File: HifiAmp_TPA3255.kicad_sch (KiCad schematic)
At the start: 123 parts, among them J1 PVDD 48V IN — NEEDS_DATA, J2 RCA L SE, J3 RCA R SE, J301 SPK_L, J302 SPK_R, J4 VOLUME_REMOTE, Q301 IPP330P10NM, Q302 IXTK200N10L2, U1 LM5010ASD, U2 LM2940IMP-12/NOPB, U3 TLV1117-33IDCY, U4 OPA1612AIDR, U5 OPA1612AIDR, U6 TPA3255B, U7 TPS3802K33DCKR, U8 LM5069-2

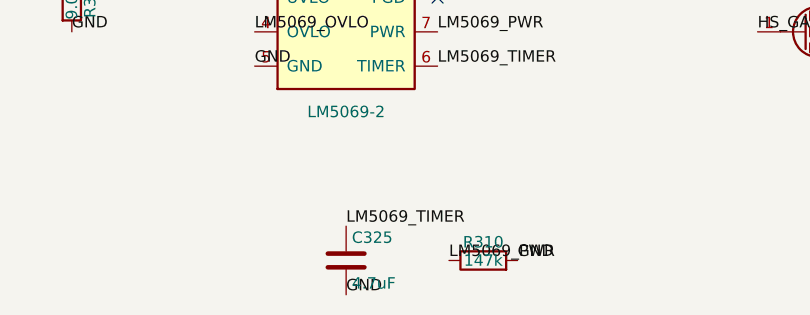
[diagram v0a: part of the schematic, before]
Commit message: fix(schematic): restore the real WIMA part for C325 and widen its footprint (D1.7)
D1.5 had rejected MKS2C044701O00KSSD as an invented part, reading the "O"
as a tolerance code. It is not one. A WIMA part number puts the box and
pitch in fields 11-12 and the tolerance in field 15 alone, so the "O" is
the second character of box code 1O and the tolerance is the "K" in KSSD.

The rejected part is the real one, and its replacement is the invented
one: B0 is not a WIMA voltage code (MKS2 spans 63 to 630 VDC with no 50 V
rating) and box 1K, 7.2 x 13 mm, only holds 2.2 uF.

Reading the catalogue also breaks the dimension assumption. At 5 mm pitch
the constant of the MKS2 series is the LENGTH, 7.2 mm, never the
thickness. The 4.7 uF box is 11 x 18 x 7.2 mm, so the W7.2mm footprint
was 3.8 mm too narrow and the part would not have fitted.

C325 now carries MKS2C044701O00KSSD, value 4.7uF/63V, and the stock
footprint C_Rect_L7.2mm_W11.0mm_P5.00mm_FKS2_FKP2_MKS2_MKP2. The x1.41
startup margin holds: +/-10 % is catalogued, only the voltage rating
moves from 50 to 63 V. Written through the MCP, re-read from the file,
position untouched, ERC still 15 warnings and 0 errors.

Two consequences recorded. D1.9 opens: C321-C324 carry the same class of
defect, a 3.5 mm box that cannot hold 680 nF at the 100 V TI requires.
D1.8 loses its blocker, since the local film footprint was redundant with
a stock one all along and only has to be dropped, never repaired.

Co-Authored-By: Claude Opus 5 <noreply@anthropic.com>
Claude-Session: https://claude.ai/code/session_019Lx21MypvErSrEbffS7PFZ
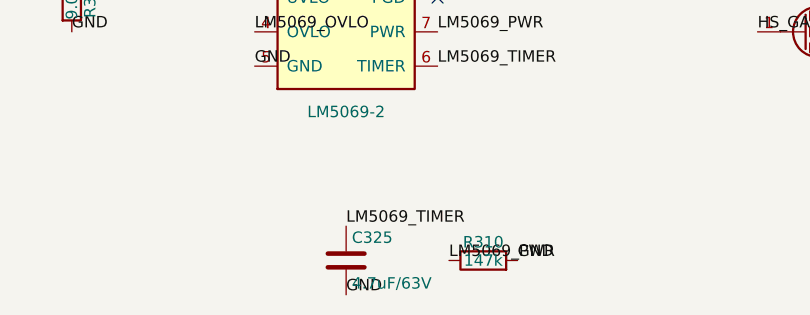
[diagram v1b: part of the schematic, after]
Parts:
- C325: value 4.7uF -> 4.7uF/63V; footprint Capacitor_THT:C_Rect_L7.2mm_W7.2mm_P5.00mm_FKS2_FKP2_MKS2_MKP2 -> Capacitor_THT:C_Rect_L7.2mm_W11.0mm_P5.00mm_FKS2_FKP2_MKS2_MKP2; MPN MKS2B044701K00KSSD -> MKS2C044701O00KSSD
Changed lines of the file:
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@@
 			)
 		)
-		(property "Value" "4.7uF"
+		(property "Value" "4.7uF/63V"
 			(at 330.835 452.12 0)
 			(effects
@@
 			)
 		)
-		(property "Footprint" "Capacitor_THT:C_Rect_L7.2mm_W7.2mm_P5.00mm_FKS2_FKP2_MKS2_MKP2"
+		(property "Footprint" "Capacitor_THT:C_Rect_L7.2mm_W11.0mm_P5.00mm_FKS2_FKP2_MKS2_MKP2"
 			(at 331.1652 453.39 0)
 			(hide yes)
@@
 			)
 		)
-				(property "MPN" "MKS2B044701K00KSSD"
+				(property "MPN" "MKS2C044701O00KSSD"
 			(at 330.2 449.58 0)
 			(effects (font (size 1.27 1.27)) (hide yes))

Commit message: fix(schematic): give the four 1500 uF bulks the diameter the EVM actually uses (D1.11)
C312 to C315 carried CP_Radial_D16.0mm_P7.50mm. The TPA3255EVM bill of
materials, which docs/architecture.md names as the anchor for this bulk,
lists EEU-FC1J152 in an 18 mm diameter can. The footprint was 2 mm too
narrow -- the fourth footprint in this project resting on a dimension that
was assumed rather than read.

C316 and C317 came out clean: the EVM lists SLPX472M080H3P3, "D35 mm x
L30", the CDE type SLP part-number key resolves H3 to 35 x 30 mm, and the
CDE mounting-hole drawing prescribes a 10.0 mm pitch with two 2.0 mm
holes -- so the KiCad 2.0 mm drill is the prescribed hole, not a zero
clearance on a 2.0 mm pin.

Footprint write read back from the file, positions untouched, ERC still at
15 violations and 0 errors.

Co-Authored-By: Claude Opus 5 <noreply@anthropic.com>
Claude-Session: https://claude.ai/code/session_01SP8MCxRp77nUWzHqJxRtmC
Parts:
- C312, C313, C314, C315: footprint Capacitor_THT:CP_Radial_D16.0mm_P7.50mm -> Capacitor_THT:CP_Radial_D18.0mm_P7.50mm
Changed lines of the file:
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@@
 			)
 		)
-		(property "Footprint" "Capacitor_THT:CP_Radial_D16.0mm_P7.50mm"
+		(property "Footprint" "Capacitor_THT:CP_Radial_D18.0mm_P7.50mm"
 			(at 394.6652 303.53 0)
 			(hide yes)
@@
 			)
 		)
-		(property "Footprint" "Capacitor_THT:CP_Radial_D16.0mm_P7.50mm"
+		(property "Footprint" "Capacitor_THT:CP_Radial_D18.0mm_P7.50mm"
 			(at 407.3652 303.53 0)
 			(hide yes)
@@
 			)
 		)
-		(property "Footprint" "Capacitor_THT:CP_Radial_D16.0mm_P7.50mm"
+		(property "Footprint" "Capacitor_THT:CP_Radial_D18.0mm_P7.50mm"
 			(at 420.0652 303.53 0)
 			(hide yes)
@@
 			)
 		)
-		(property "Footprint" "Capacitor_THT:CP_Radial_D16.0mm_P7.50mm"
+		(property "Footprint" "Capacitor_THT:CP_Radial_D18.0mm_P7.50mm"
 			(at 432.7652 303.53 0)
 			(hide yes)

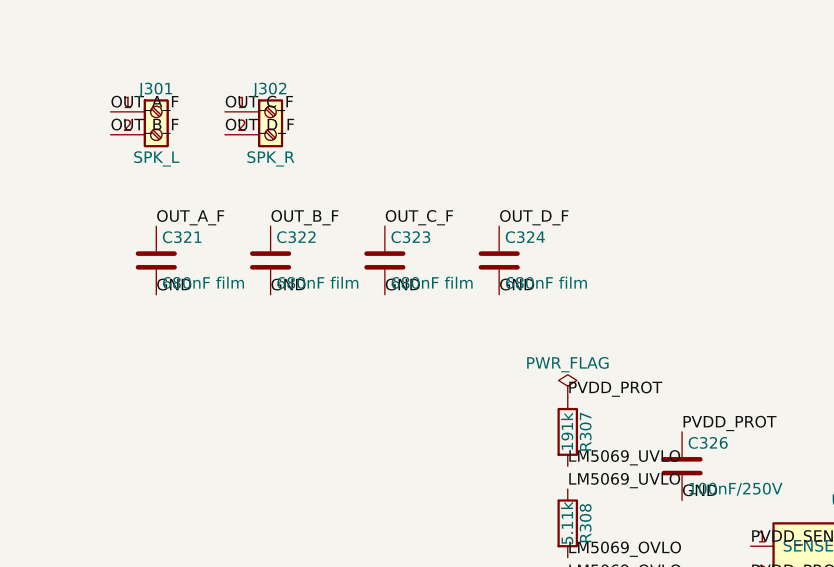
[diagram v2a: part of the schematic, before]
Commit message: fix(schematic): put the output-filter films on the box WIMA actually sells (D1.9)
C321 to C324 carried a 5 mm pitch footprint for a 7.2 x 3.5 mm body. Both
figures were wrong. The TPA3255EVM bill of materials settles the dielectric
first: the EVM uses a KEMET PHE426HB7100JR06, metallized polypropylene,
1 uF/250 V on a 17.5 mm pitch. The WIMA MKP4 catalogue then contradicts the
assumption that no MKP exists below 250 V -- the series starts at 100 VDC --
and lists 0.68 uF in an 8 x 15 x 18 mm box on a 15 mm pitch, the same box at
100 and at 250 VDC. 250 V costs nothing mechanically, so it is what we take.

The four caps move to Capacitor_THT:C_Rect_L18.0mm_W8.0mm_P15.00mm_FKS3_FKP3,
a standard-library footprint whose own description points back at the WIMA
catalogue, and their Value now carries the rating.

This leaves CF_Film_Box_P5.00mm_7.2x3.5mm with no users, so it goes. The
local library keeps only the fuse, and its fp-lib-table entry stays earned.

Writes read back from the file, positions untouched, ERC still at 15
violations and 0 errors with the same message set.

Co-Authored-By: Claude Opus 5 <noreply@anthropic.com>
Claude-Session: https://claude.ai/code/session_01SP8MCxRp77nUWzHqJxRtmC
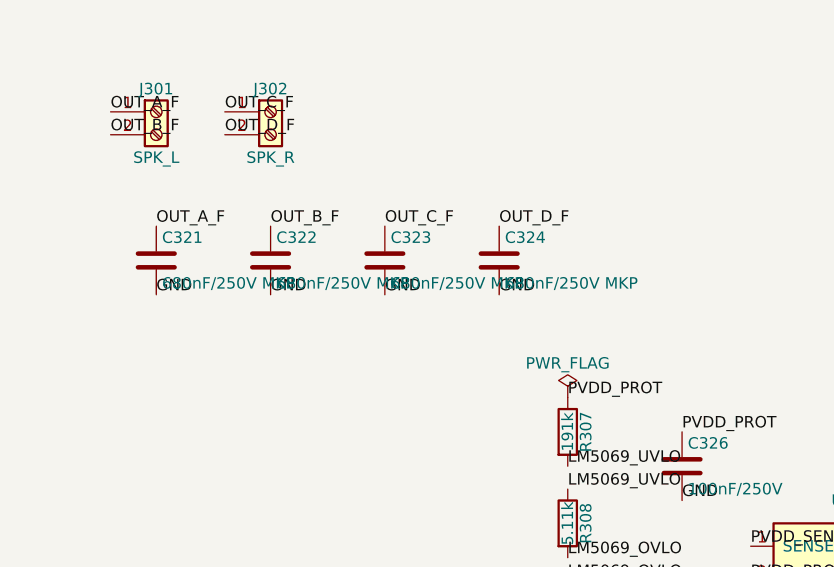
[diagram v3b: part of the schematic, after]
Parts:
- C321, C322, C323, C324: value 680nF film -> 680nF/250V MKP; footprint HifiAmp_TPA3255_Local:CF_Film_Box_P5.00mm_7.2x3.5mm -> Capacitor_THT:C_Rect_L18.0mm_W8.0mm_P15.00mm_FKS3_FKP3
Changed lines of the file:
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@@
 			)
 		)
-		(property "Value" "680nF film"
+		(property "Value" "680nF/250V MKP"
 			(at 254.635 383.54 0)
 			(effects
@@
 			)
 		)
-		(property "Footprint" "HifiAmp_TPA3255_Local:CF_Film_Box_P5.00mm_7.2x3.5mm"
+		(property "Footprint" "Capacitor_THT:C_Rect_L18.0mm_W8.0mm_P15.00mm_FKS3_FKP3"
 			(at 254.9652 384.81 0)
 			(hide yes)
@@
 			)
 		)
-		(property "Value" "680nF film"
+		(property "Value" "680nF/250V MKP"
 			(at 267.335 383.54 0)
 			(effects
@@
 			)
 		)
-		(property "Footprint" "HifiAmp_TPA3255_Local:CF_Film_Box_P5.00mm_7.2x3.5mm"
+		(property "Footprint" "Capacitor_THT:C_Rect_L18.0mm_W8.0mm_P15.00mm_FKS3_FKP3"
 			(at 267.6652 384.81 0)
 			(hide yes)
@@
 			)
 		)
-		(property "Value" "680nF film"
+		(property "Value" "680nF/250V MKP"
 			(at 280.035 383.54 0)
 			(effects
@@
 			)
 		)
-		(property "Footprint" "HifiAmp_TPA3255_Local:CF_Film_Box_P5.00mm_7.2x3.5mm"
+		(property "Footprint" "Capacitor_THT:C_Rect_L18.0mm_W8.0mm_P15.00mm_FKS3_FKP3"
 			(at 280.3652 384.81 0)
 			(hide yes)
@@
 			)
 		)
-		(property "Value" "680nF film"
+		(property "Value" "680nF/250V MKP"
 			(at 292.735 383.54 0)
 			(effects
@@
 			)
 		)
-		(property "Footprint" "HifiAmp_TPA3255_Local:CF_Film_Box_P5.00mm_7.2x3.5mm"
+		(property "Footprint" "Capacitor_THT:C_Rect_L18.0mm_W8.0mm_P15.00mm_FKS3_FKP3"
 			(at 293.0652 384.81 0)
 			(hide yes)

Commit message: feat(schematic): settle the output inductors on a real part (D1.10, D1.12)
L301 to L304 carried Inductor_SMD:L_Wuerth_HCI-1350 with no MPN behind it,
and the stored-energy argument said that can was about half the size the
job needs. The TPA3255EVM bill of materials points at Coilcraft's MA5172-AE,
and that datasheet (document 943) lists PA6331-AE in the same family:
15 uH, 31 mOhm DCR, 20 A Isat, 9.8 A Irms at a 20 C rise. That is our spec
sheet, on a part built for TI Class-D stages. Taken on the user's call.

The real part is a 28.6 x 12.3 mm through-hole toroid standing upright, not
a 12.8 mm SMD can. The datasheet drawing is not to scale -- 2.836 pt/mm in
the front view against 2.463 in profile -- so the labels rule, as with
Schurter: 10.0 +/- 0.5 mm pin spacing, 0.96 to 1.07 mm pins.

No standard footprint fits. Bourns_5700 has the length but an 11.43 mm
spacing, past tolerance; Pulse_D has the spacing but a courtyard 1.9 mm too
short. So the project earns a second local footprint. This time
create_footprint's own graphics came out right -- 0.25 mm around the
outermost feature, silkscreen 0.15 mm clear of the body. CF_Film_Box failed
because of the dimensions it was handed, not because of the generator.

D1.12: fp-lib-table named the local library by an absolute Windows path, so
a clone of this repo anywhere else would have lost both local footprints
without a word. It now uses ${KIPRJMOD}, which sym-lib-table already did.

Footprint and writes read back from the files, ERC still at 15 violations
and 0 errors.

Co-Authored-By: Claude Opus 5 <noreply@anthropic.com>
Claude-Session: https://claude.ai/code/session_01SP8MCxRp77nUWzHqJxRtmC
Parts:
- L301, L302, L303, L304: value 15uH -> 15uH/20A; footprint Inductor_SMD:L_Wuerth_HCI-1350 -> HifiAmp_TPA3255_Local:L_Toroid_Vertical_L28.6mm_W12.3mm_P10.00mm_Coilcraft_PA6331
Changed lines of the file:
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@@
 			)
 		)
-		(property "Value" "15uH"
+		(property "Value" "15uH/20A"
 			(at 255.905 345.44 90)
 			(effects
@@
 			)
 		)
-		(property "Footprint" "Inductor_SMD:L_Wuerth_HCI-1350"
+		(property "Footprint" "HifiAmp_TPA3255_Local:L_Toroid_Vertical_L28.6mm_W12.3mm_P10.00mm_Coilcraft_PA6331"
 			(at 254 345.44 0)
 			(hide yes)
@@
 			)
 		)
-		(property "Value" "15uH"
+		(property "Value" "15uH/20A"
 			(at 268.605 345.44 90)
 			(effects
@@
 			)
 		)
-		(property "Footprint" "Inductor_SMD:L_Wuerth_HCI-1350"
+		(property "Footprint" "HifiAmp_TPA3255_Local:L_Toroid_Vertical_L28.6mm_W12.3mm_P10.00mm_Coilcraft_PA6331"
 			(at 266.7 345.44 0)
 			(hide yes)
@@
 			)
 		)
-		(property "Value" "15uH"
+		(property "Value" "15uH/20A"
 			(at 281.305 345.44 90)
 			(effects
@@
 			)
 		)
-		(property "Footprint" "Inductor_SMD:L_Wuerth_HCI-1350"
+		(property "Footprint" "HifiAmp_TPA3255_Local:L_Toroid_Vertical_L28.6mm_W12.3mm_P10.00mm_Coilcraft_PA6331"
 			(at 279.4 345.44 0)
 			(hide yes)
@@
 			)
 		)
-		(property "Value" "15uH"
+		(property "Value" "15uH/20A"
 			(at 294.005 345.44 90)
 			(effects
@@
 			)
 		)
-		(property "Footprint" "Inductor_SMD:L_Wuerth_HCI-1350"
+		(property "Footprint" "HifiAmp_TPA3255_Local:L_Toroid_Vertical_L28.6mm_W12.3mm_P10.00mm_Coilcraft_PA6331"
 			(at 292.1 345.44 0)
 			(hide yes)

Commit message: fix(schematic): put U6 on the package the TPA3255 actually ships in (D1.3)
U6 carried HTSSOP-44-1EP_..._EP5.2x14mm, which is tagged Texas_DDW0044B --
a different package. It puts a 45th pad, 5.2 x 14 mm, underneath the chip.
The TPA3255 is DDV0044D, and the datasheet says plainly that its PowerPAD
"is located on the top side of the device for convenient thermal coupling
to the heat sink". TI's own land pattern shows 44 pads and nothing to
solder underneath; the package outline gives the exposed pad as 7.01 x 4.14
mm nominal, not 5.2 x 14.

So the task inverts: there are no thermal vias to design under this part.
The numbers say it outright -- RthetaJC(bot) is listed n/a, while RthetaJA
drops from 50.7 to 2.4 C/W once a heatsink sits on top. The NEEDS_DATA that
expected a 5.2 x 14 mm pad is disproved, not confirmed, and the heatsink is
now the only thing sizing this chip's thermals.

Known and deliberate: the symbol has 45 pins, pin 45 being EP_45 wired to
GND, which is what TI asks for, while the footprint has 44 pads. The PCB
import will flag a pin with no pad. That is correct here -- the PowerPAD's
ground path runs through the heatsink, off the board.

Two findings opened rather than fixed. D1.13: TI caps PVDD at 53.5 V
absolute into 4 ohms, but the LM5069 only cuts at 56.4 V, so a 4 ohm load
sits out of spec between the two with nothing intervening. D1.14: the five
lib_symbol_mismatch warnings are a third of the C2 baseline and have never
been diagnosed -- the gap could be a property field or a pinout.

ERC still at 15 violations and 0 errors.

Co-Authored-By: Claude Opus 5 <noreply@anthropic.com>
Claude-Session: https://claude.ai/code/session_01SP8MCxRp77nUWzHqJxRtmC
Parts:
- U6: footprint Package_SO:HTSSOP-44-1EP_6.1x14mm_P0.635mm_EP5.2x14mm_Mask4.31x8.26mm -> Package_SO:HTSSOP-44_6.1x14mm_P0.635mm_TopEP4.14x7.01mm
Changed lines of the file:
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@@
 			)
 		)
-		(property "Footprint" "Package_SO:HTSSOP-44-1EP_6.1x14mm_P0.635mm_EP5.2x14mm_Mask4.31x8.26mm"
+		(property "Footprint" "Package_SO:HTSSOP-44_6.1x14mm_P0.635mm_TopEP4.14x7.01mm"
 			(at 340.36 180.34 0)
 			(hide yes)

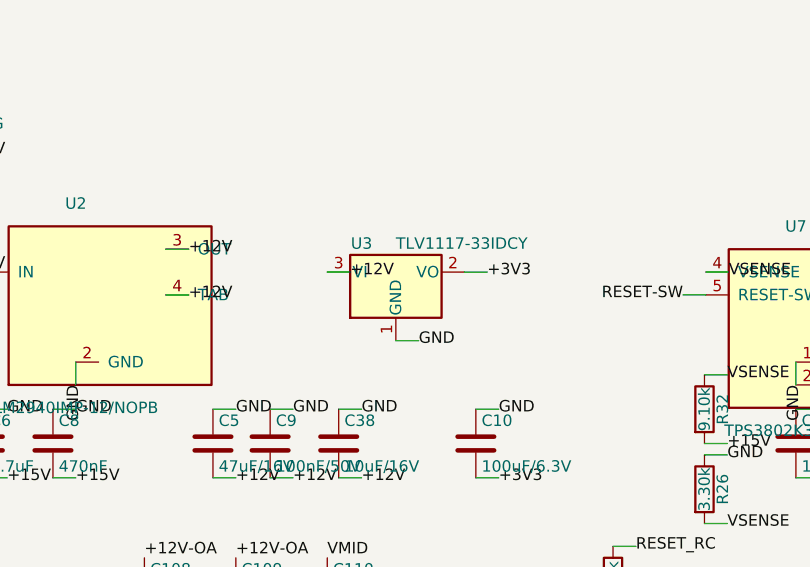
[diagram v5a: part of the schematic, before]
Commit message: fix(e1.8): give U3's tab a net by stacking a fourth pin on the output
The SOT-223 tab was floating because the stock Regulator_Linear:TLV1117-33
symbol declares three pins where the DCY package has four. A local
TLV1117_33_FIXED now carries a fourth pin, TAB, typed passive and placed at
exactly the same coordinates and length as pin 2, VO. U3 points at it without
moving: same position, same UUID, same Reference, Value and Footprint.

Stacking rather than a separate anchor is deliberate, and it departs from the
LM2940IMP_12_FIXED precedent on purpose. The tab is electrically the same node
as the output, so stacking connects it with no wire and no label - and above
all with no anchor coordinate to compute, which was the one genuinely fallible
part of the job. Deriving KiCad's pin-anchor convention from the file turned
out not to be straightforward, and this sidesteps it entirely. Typing the pin
passive avoids a power_out against power_out conflict in ERC.

Proven at the file: U3 pad 4 carries /+3V3, and no numbered pad anywhere on
the board is left without a net. The 21 placements from E1.2 are untouched,
122 footprints, 74 nets, outline intact, schematic_parity still 0. Unconnected
items go from 253 to 254 - exactly the pad that just gained a net and is not
routed yet, which is the arithmetic proof the connection took.

One cost, stated rather than hidden: ERC moves from 15 violations to 16, still
zero errors. The extra one is a lib_symbol_mismatch joining the five the
project already carries for its other local symbols - a formatting difference
between the schematic's cached copy and the library's, with no electrical
meaning. GATE C2's baseline is therefore 16/0 from here on.

Also recorded, after it cost a full automation run: KiCad must not be launched
from the agent's shell. That shell is elevated, KiCad inherits the admin
token, and UIPI then silently drops every click and keystroke from a
non-elevated automation session while the calls still report success. Lau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
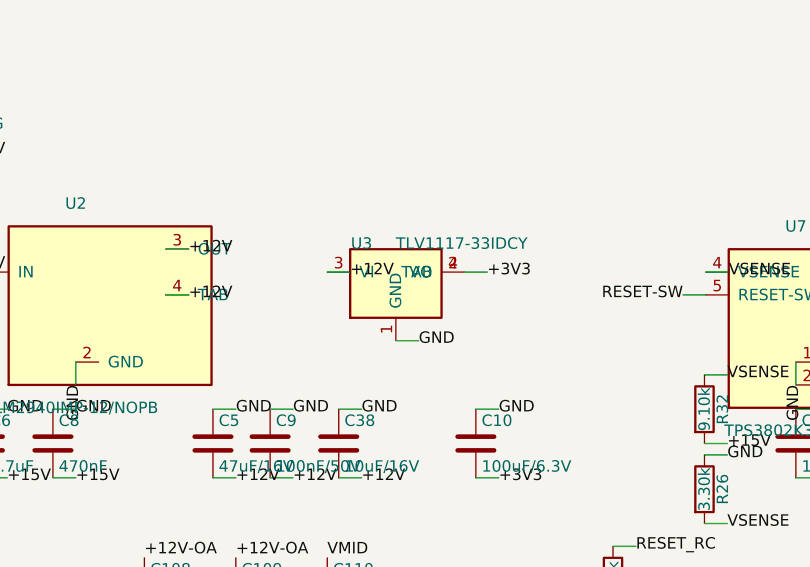
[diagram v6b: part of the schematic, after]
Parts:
- U3: symbol Regulator_Linear:TLV1117-33 -> HifiAmp_TPA3255_Local:TLV1117_33_FIXED
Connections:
- net +3V3: now also U3.4 (TAB)
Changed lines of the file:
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@@
 	)
 	(symbol
-		(lib_id "Regulator_Linear:TLV1117-33")
+		(lib_id "HifiAmp_TPA3255_Local:TLV1117_33_FIXED")
 		(at 195.58 100.33 0)
 		(unit 1)
